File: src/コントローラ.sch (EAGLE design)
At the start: 37 parts

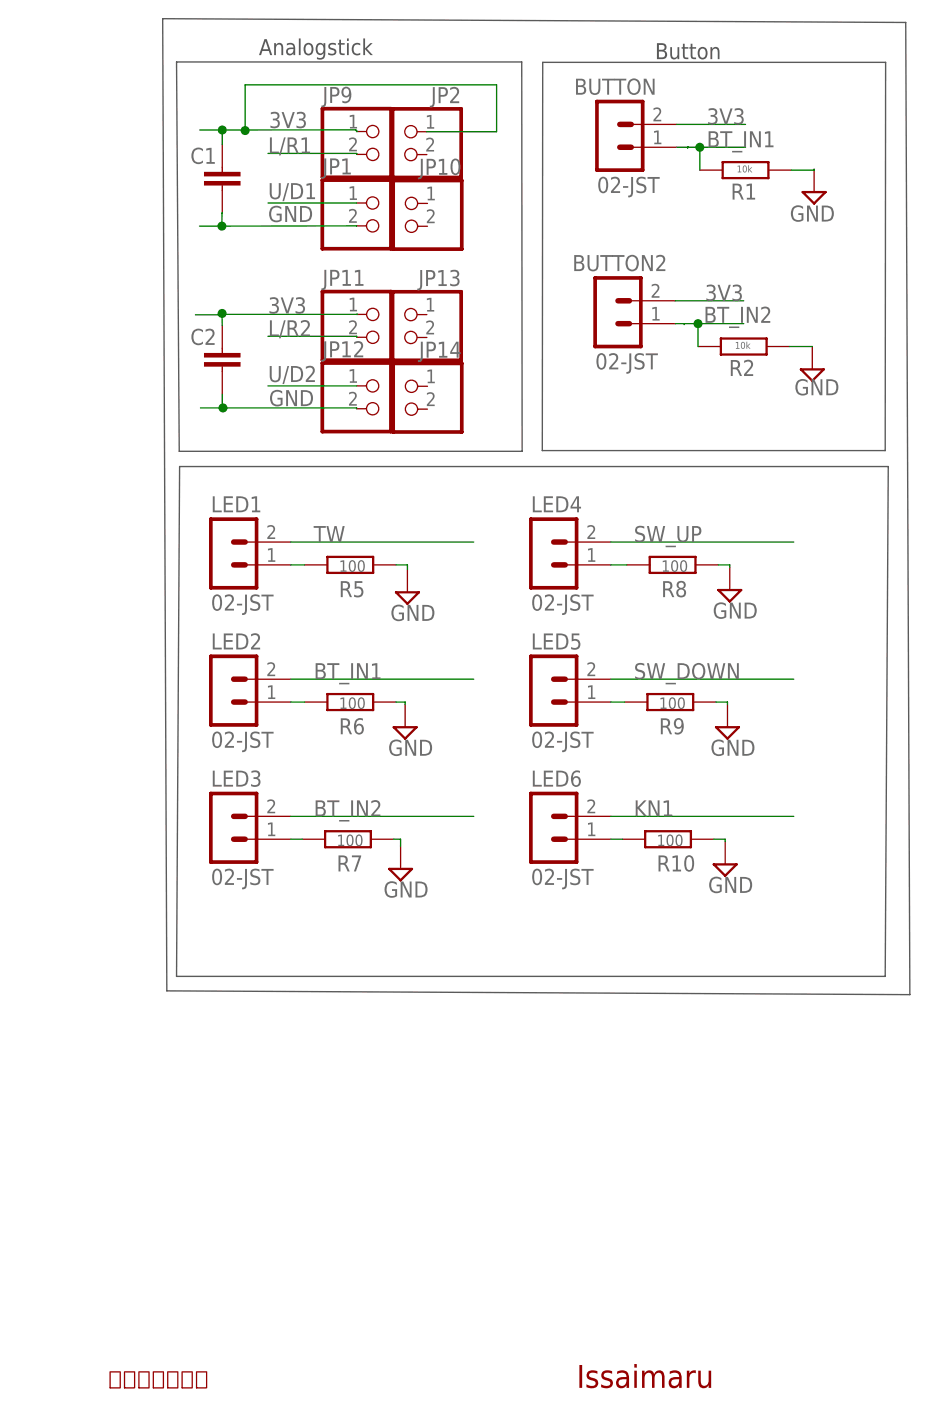
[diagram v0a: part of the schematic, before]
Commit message: 国技館コントローラの追加
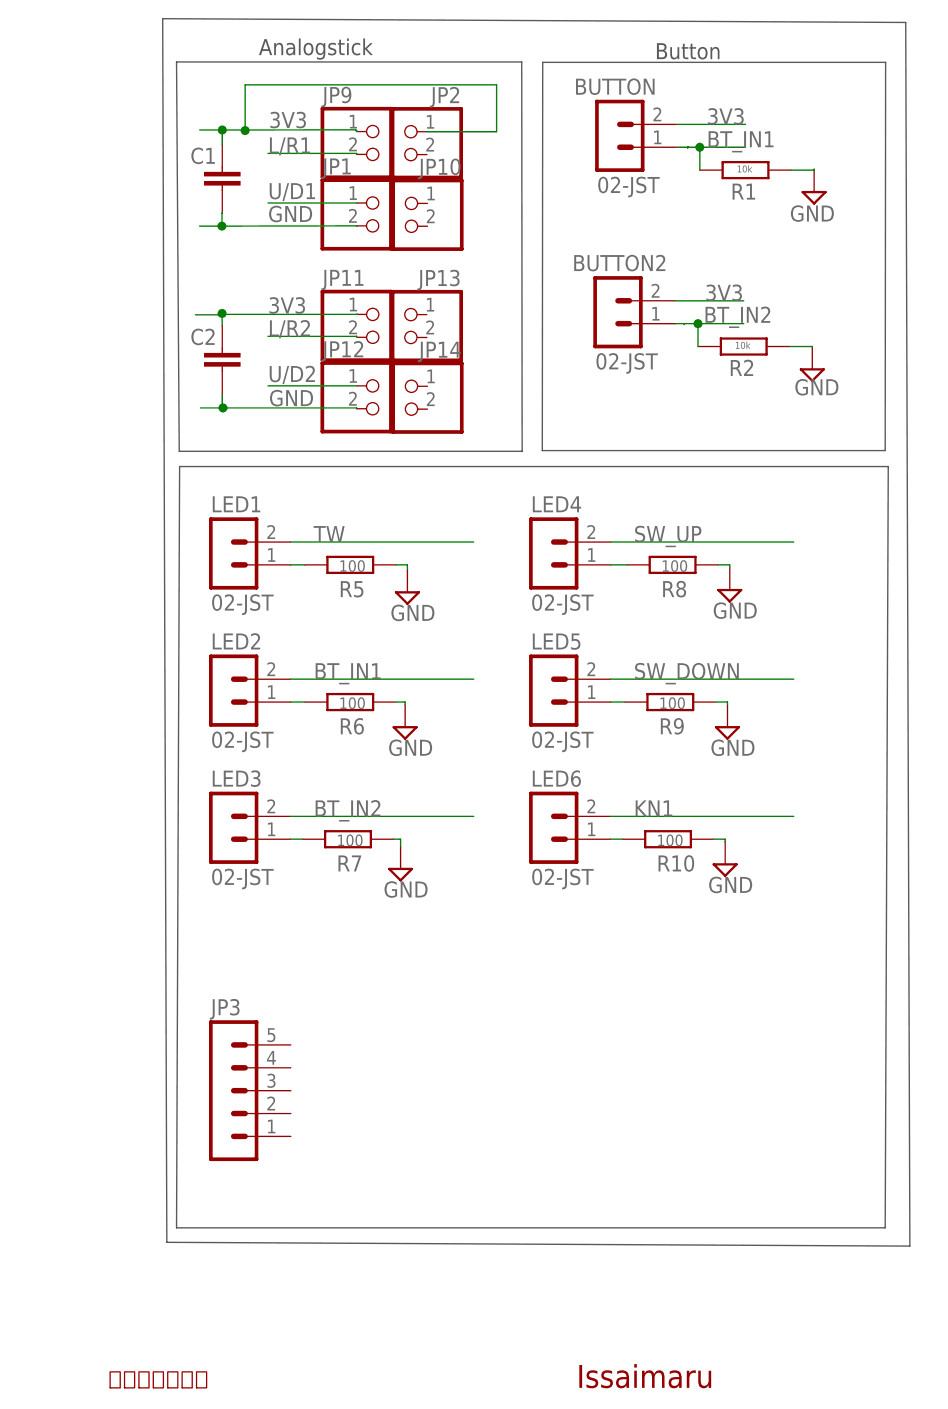
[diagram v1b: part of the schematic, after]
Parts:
- added JP3: (no value), con-jst-xh:05-JST
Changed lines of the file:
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@@
 <part name="PIN" library="pinhead" library_urn="urn:adsk.eagle:library:325" deviceset="PINHD-1X7" device="" package3d_urn="urn:adsk.eagle:package:22477/2"/>
 <part name="PINSOCKET" library="pinhead" library_urn="urn:adsk.eagle:library:325" deviceset="PINHD-1X7" device="" package3d_urn="urn:adsk.eagle:package:22477/2"/>
+<part name="JP3" library="con-jst-xh" deviceset="05-JST" device=""/>
 </parts>
 <sheets>
@@
 <text x="102.332" y="110.2" size="2.54" layer="97" rot="MR0">MCU</text>
 <text x="165.1" y="20.32" size="1.778" layer="94">モジュール一覧</text>
-<wire x1="171.18" y1="172.45" x2="171.64" y2="64.43" width="0.1524" layer="97"/>
-<wire x1="171.64" y1="64.43" x2="254.2" y2="64.01" width="0.1524" layer="97"/>
-<wire x1="254.2" y1="64.01" x2="253.74" y2="172.03" width="0.1524" layer="97"/>
+<wire x1="171.18" y1="172.45" x2="171.64" y2="36.49" width="0.1524" layer="97"/>
+<wire x1="171.64" y1="36.49" x2="254.2" y2="36.07" width="0.1524" layer="97"/>
+<wire x1="254.2" y1="36.07" x2="253.74" y2="172.03" width="0.1524" layer="97"/>
 <wire x1="253.74" y1="172.03" x2="171.18" y2="172.45" width="0.1524" layer="97"/>
 <text x="165.1" y="15.24" size="1.778" layer="94">スティック 2</text>
@@
 <wire x1="127" y1="99.06" x2="68.58" y2="99.06" width="0.1524" layer="97"/>
 <wire x1="173.06" y1="122.688" x2="251.8" y2="122.688" width="0.1524" layer="97"/>
-<wire x1="251.8" y1="122.688" x2="251.46" y2="66.04" width="0.1524" layer="97"/>
-<wire x1="251.46" y1="66.04" x2="172.72" y2="66.04" width="0.1524" layer="97"/>
-<wire x1="172.72" y1="66.04" x2="173.06" y2="122.688" width="0.1524" layer="97"/>
+<wire x1="251.8" y1="122.688" x2="251.46" y2="38.1" width="0.1524" layer="97"/>
+<wire x1="251.46" y1="38.1" x2="172.72" y2="38.1" width="0.1524" layer="97"/>
+<wire x1="172.72" y1="38.1" x2="173.06" y2="122.688" width="0.1524" layer="97"/>
 <text x="181.864" y="168.402" size="1.778" layer="97">Analogstick</text>
 <text x="225.882" y="167.952" size="1.778" layer="97">Button</text>
@@
 <attribute name="VALUE" x="25.146" y="61.468" size="1.778" layer="96"/>
 </instance>
+<instance part="JP3" gate="G$1" x="177.8" y="53.34" smashed="yes">
+<attribute name="VALUE" x="176.53" y="43.18" size="1.778" layer="96"/>
+<attribute name="NAME" x="176.53" y="61.722" size="1.778" layer="95"/>
+</instance>
 </instances>
